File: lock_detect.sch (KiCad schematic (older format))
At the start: 9 parts, among them U10 LM339, U6 74HC86

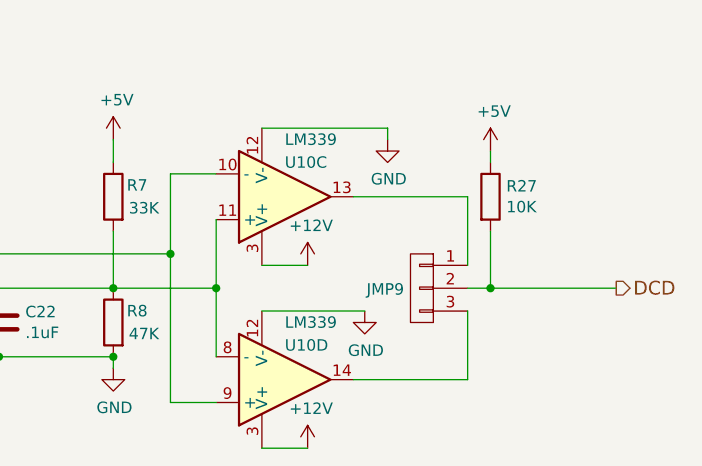
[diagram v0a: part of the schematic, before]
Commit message: Final parts placement and verified net against an actual Issue 3 board.
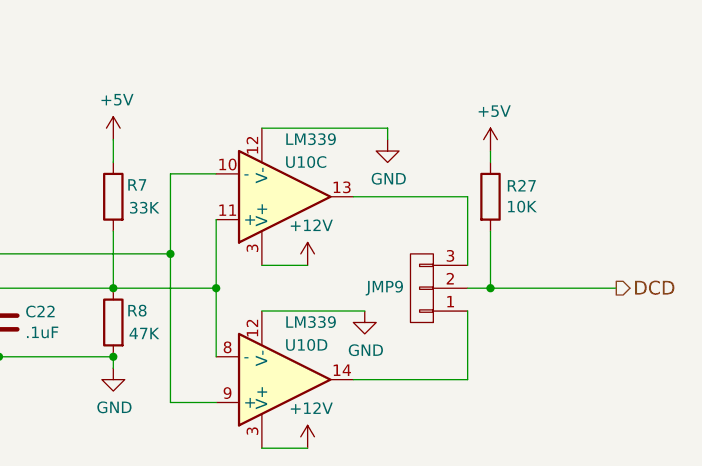
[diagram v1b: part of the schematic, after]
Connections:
- net at U10.13: now also JMP9.3 (P3); no longer JMP9.1 (P1)
- net at U10.14: now also JMP9.1 (P1); no longer JMP9.3 (P3)
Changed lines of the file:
@@
 F 3 "" H 7250 3750 50  0001 C CNN
 	1    7250 3750
-	-1   0    0    -1
+	-1   0    0    1
 $EndComp
 $Comp
